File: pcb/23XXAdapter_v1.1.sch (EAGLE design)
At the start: 29 parts, among them IC1 23XX, IC2 EPROM, IC3 74HCT138N

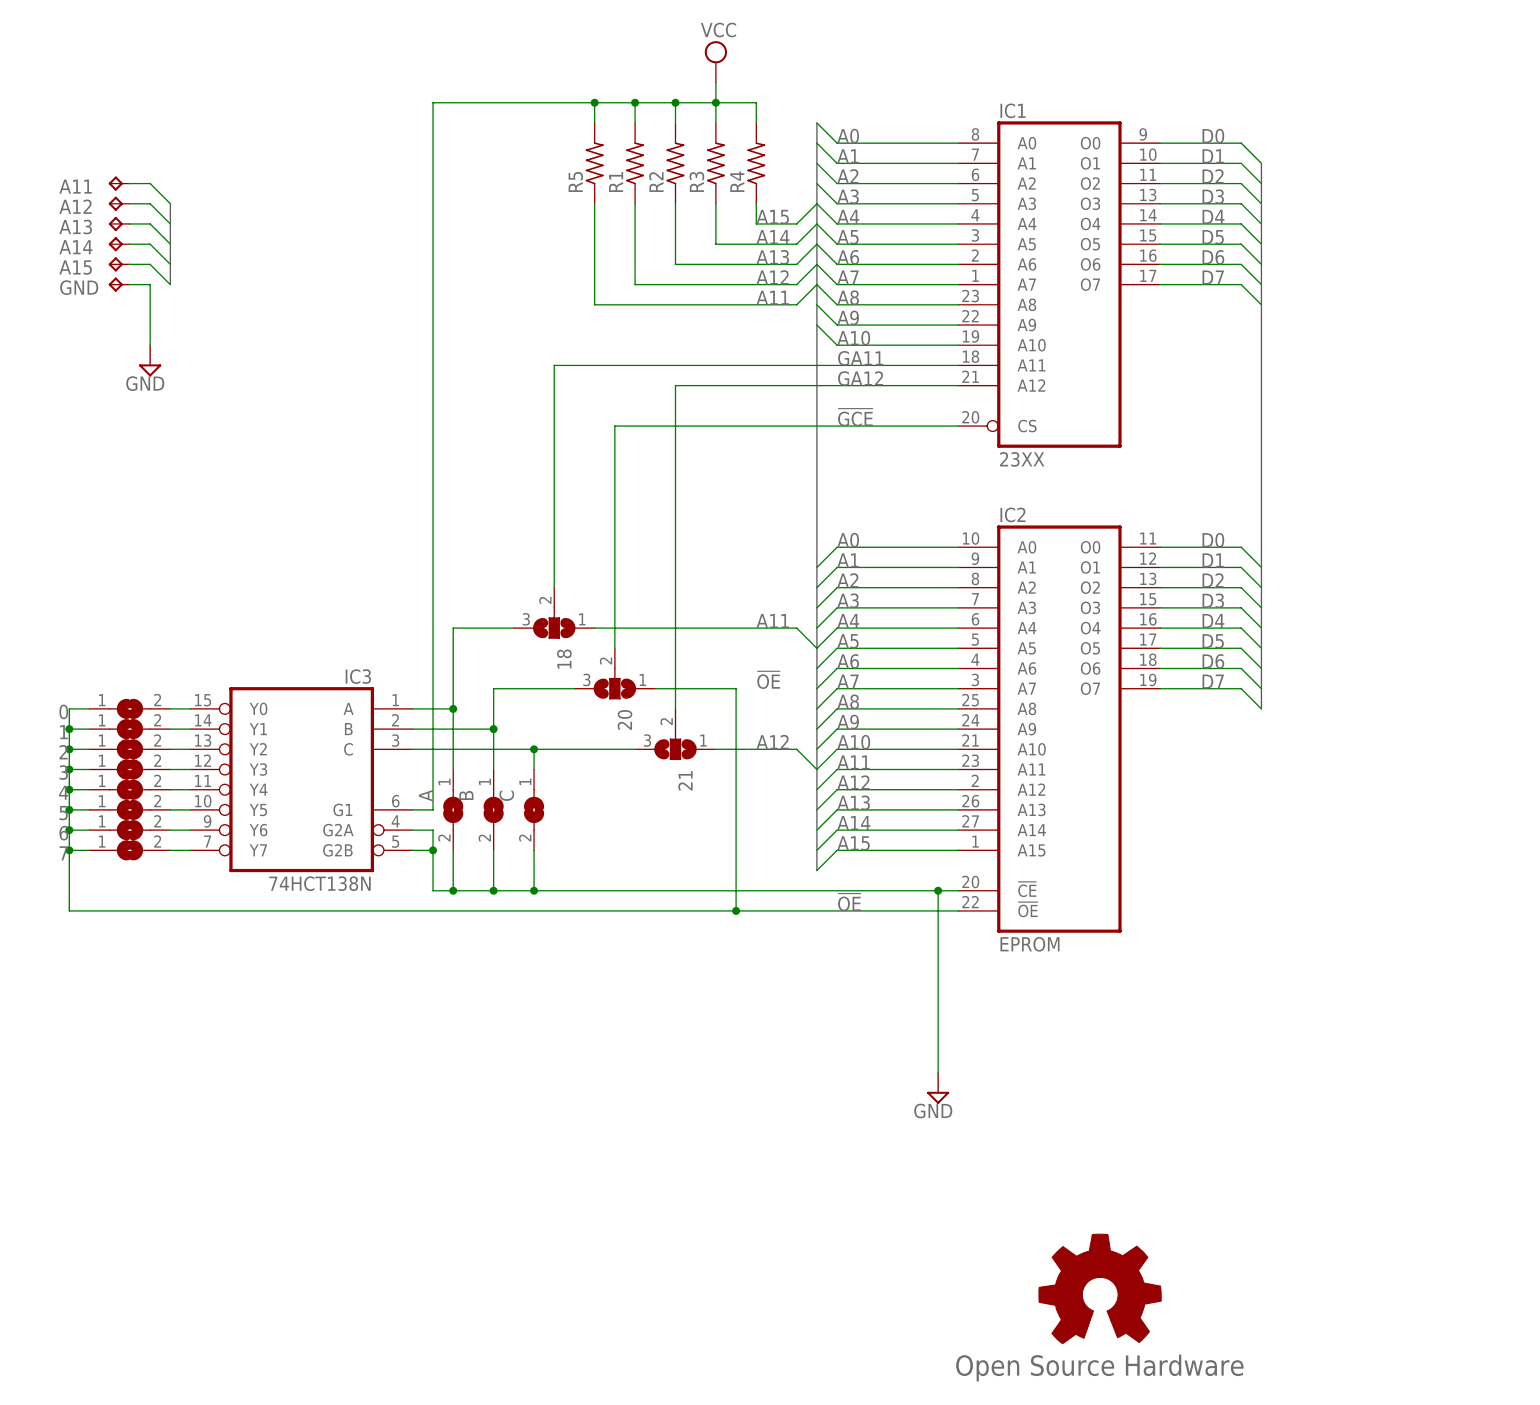
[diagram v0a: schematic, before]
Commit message: Added BOM and updates to PCB
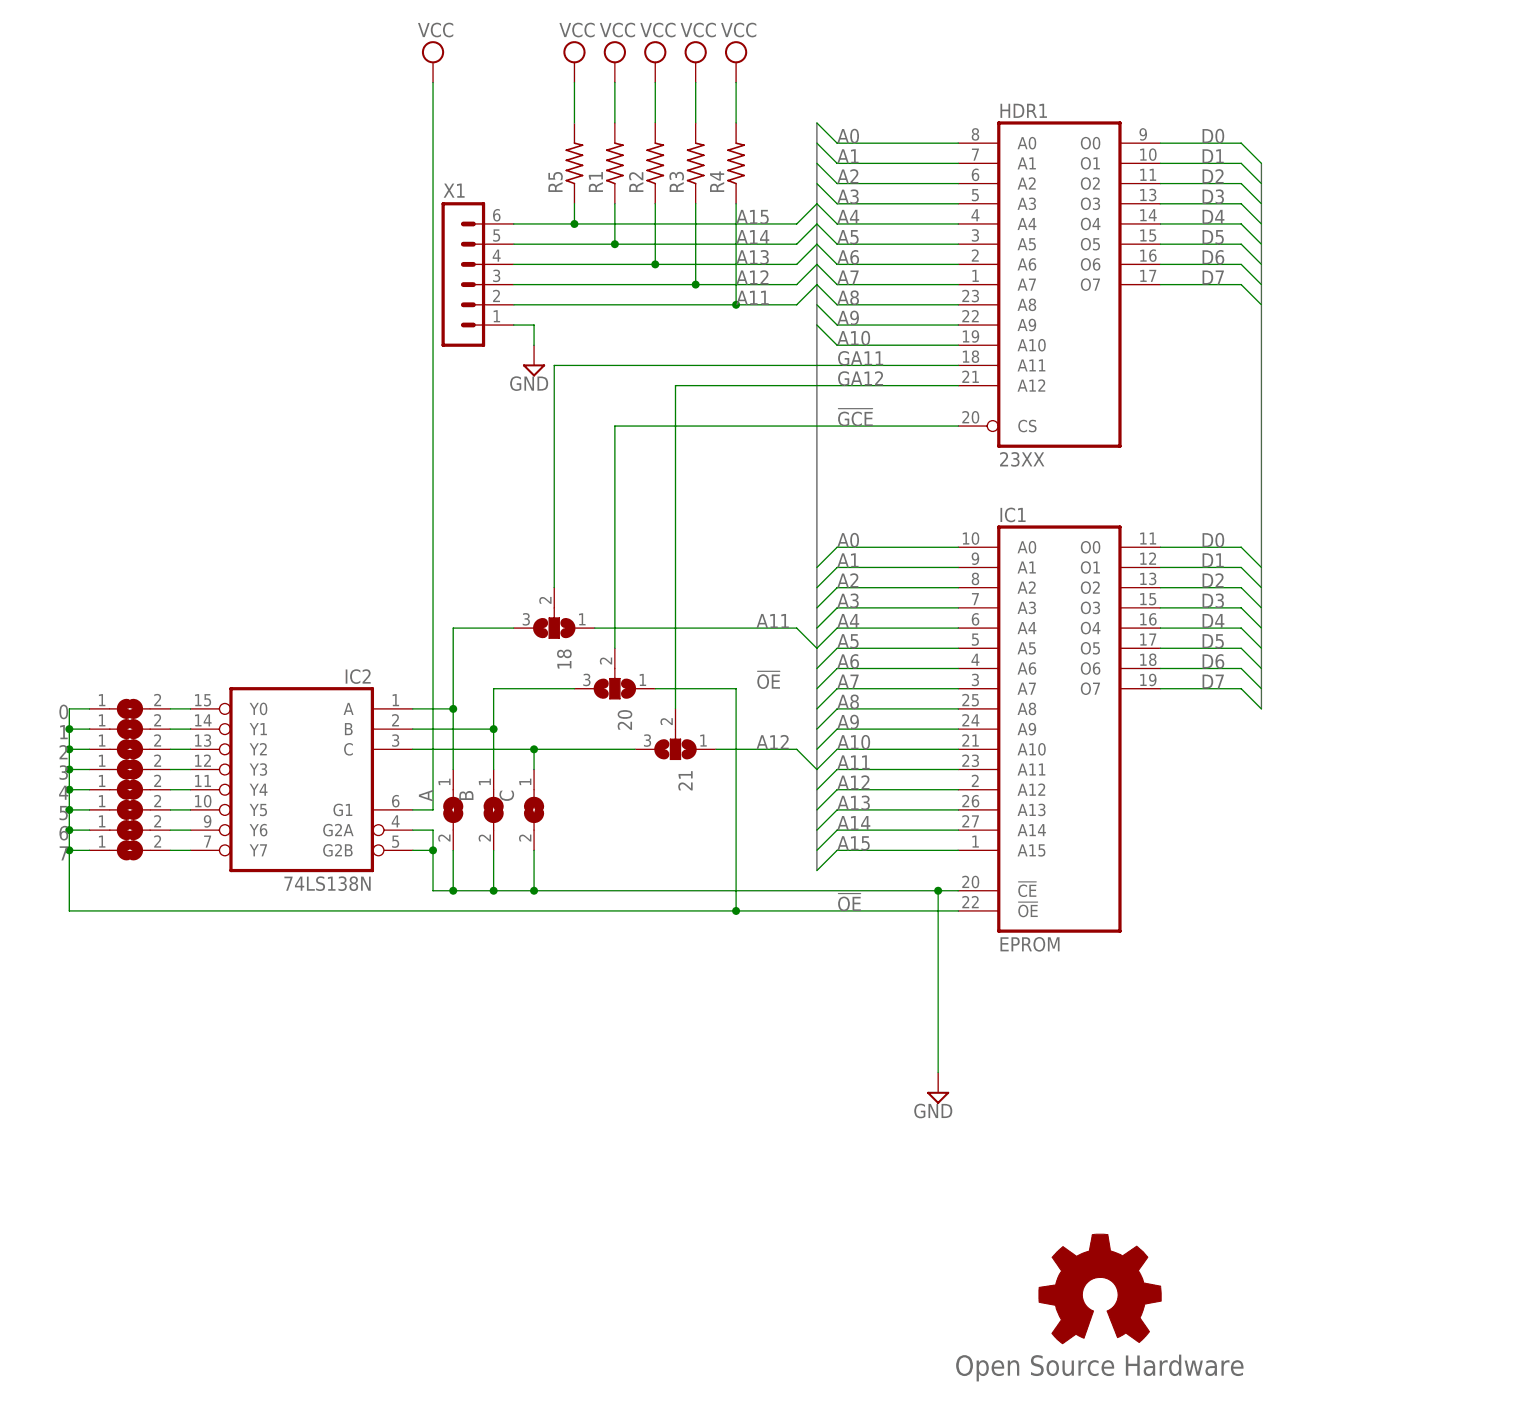
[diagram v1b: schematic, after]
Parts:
- removed A11, A12, A13, A14, A15, GND: TPTP12R, testpad:TPTP12R
- removed IC3: 74HCT138N, 74xx-us:74LS138N
- added HDR1: 23XX, 0RB_Memory:2364'RD'
- added X1: (no value), con-lstb-rp:MA06-1
- IC1: value 23XX -> EPROM; device 0RB_Memory:2364'RD' -> 0RB_Memory:27512'RD'
- IC2: value EPROM -> 74LS138N; device 0RB_Memory:27512'RD' -> 74xx-us-jlb:74LS138N
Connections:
- net !GCE: now also HDR1A.CS; no longer IC1A.CS
- net !OE: now also IC1G$1.!OE; no longer IC2G$1.!OE
- net A0: now also HDR1A.A0, IC1G$1.A0; no longer IC1A.A0, IC2G$1.A0
- net A1: now also HDR1A.A1, IC1G$1.A1; no longer IC1A.A1, IC2G$1.A1
- net A10: now also HDR1A.A10, IC1G$1.A10; no longer IC1A.A10, IC2G$1.A10
- net A11: now also IC1G$1.A11, X1.6; no longer A11.TP, IC2G$1.A11
- net A12: now also IC1G$1.A12, X1.5; no longer A12.TP, IC2G$1.A12
- net A13: now also IC1G$1.A13, X1.4; no longer A13.TP, IC2G$1.A13
- net A14: now also IC1G$1.A14, X1.3; no longer A14.TP, IC2G$1.A14
- net A15: now also IC1G$1.A15, X1.2; no longer A15.TP, IC2G$1.A15
- net A2: now also HDR1A.A2, IC1G$1.A2; no longer IC1A.A2, IC2G$1.A2
- net A3: now also HDR1A.A3, IC1G$1.A3; no longer IC1A.A3, IC2G$1.A3
- net A4: now also HDR1A.A4, IC1G$1.A4; no longer IC1A.A4, IC2G$1.A4
- net A5: now also HDR1A.A5, IC1G$1.A5; no longer IC1A.A5, IC2G$1.A5
- net A6: now also HDR1A.A6, IC1G$1.A6; no longer IC1A.A6, IC2G$1.A6
- net A7: now also HDR1A.A7, IC1G$1.A7; no longer IC1A.A7, IC2G$1.A7
- net A8: now also HDR1A.A8, IC1G$1.A8; no longer IC1A.A8, IC2G$1.A8
- net A9: now also HDR1A.A9, IC1G$1.A9; no longer IC1A.A9, IC2G$1.A9
- net D0: now also HDR1A.O0, IC1G$1.O0; no longer IC1A.O0, IC2G$1.O0
- net D1: now also HDR1A.O1, IC1G$1.O1; no longer IC1A.O1, IC2G$1.O1
- net D2: now also HDR1A.O2, IC1G$1.O2; no longer IC1A.O2, IC2G$1.O2
- net D3: now also HDR1A.O3, IC1G$1.O3; no longer IC1A.O3, IC2G$1.O3
- net D4: now also HDR1A.O4, IC1G$1.O4; no longer IC1A.O4, IC2G$1.O4
- net D5: now also HDR1A.O5, IC1G$1.O5; no longer IC1A.O5, IC2G$1.O5
- net D6: now also HDR1A.O6, IC1G$1.O6; no longer IC1A.O6, IC2G$1.O6
- net D7: now also HDR1A.O7, IC1G$1.O7; no longer IC1A.O7, IC2G$1.O7
- net GA11: now also HDR1A.A11; no longer IC1A.A11
- net GA12: now also HDR1A.A12; no longer IC1A.A12
- net GND: now also IC1G$1.!CE, IC2A.G2A, IC2A.G2B, X1.1; no longer GND.TP, IC2G$1.!CE, IC3A.G2A, IC3A.G2B
- net N$1: now also IC2A.B; no longer IC3A.B
- net N$10: now also IC2A.Y5; no longer IC3A.Y5
- net N$11: now also IC2A.Y6; no longer IC3A.Y6
- net N$12: now also IC2A.Y7; no longer IC3A.Y7
- net N$13: now also IC2A.C; no longer IC3A.C
- net N$16: now also IC2A.A; no longer IC3A.A
- net N$4: now also IC2A.Y0; no longer IC3A.Y0
- net N$6: now also IC2A.Y1; no longer IC3A.Y1
- net N$7: now also IC2A.Y2; no longer IC3A.Y2
- net N$8: now also IC2A.Y3; no longer IC3A.Y3
- net N$9: now also IC2A.Y4; no longer IC3A.Y4
- net VCC: now also IC2A.G1; no longer IC3A.G1
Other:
- moved on the sheet: R1, R2, R3, R4, R5

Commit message: Update schematic to show VCC/GND and pre-connected pads, h/t Mike Forster
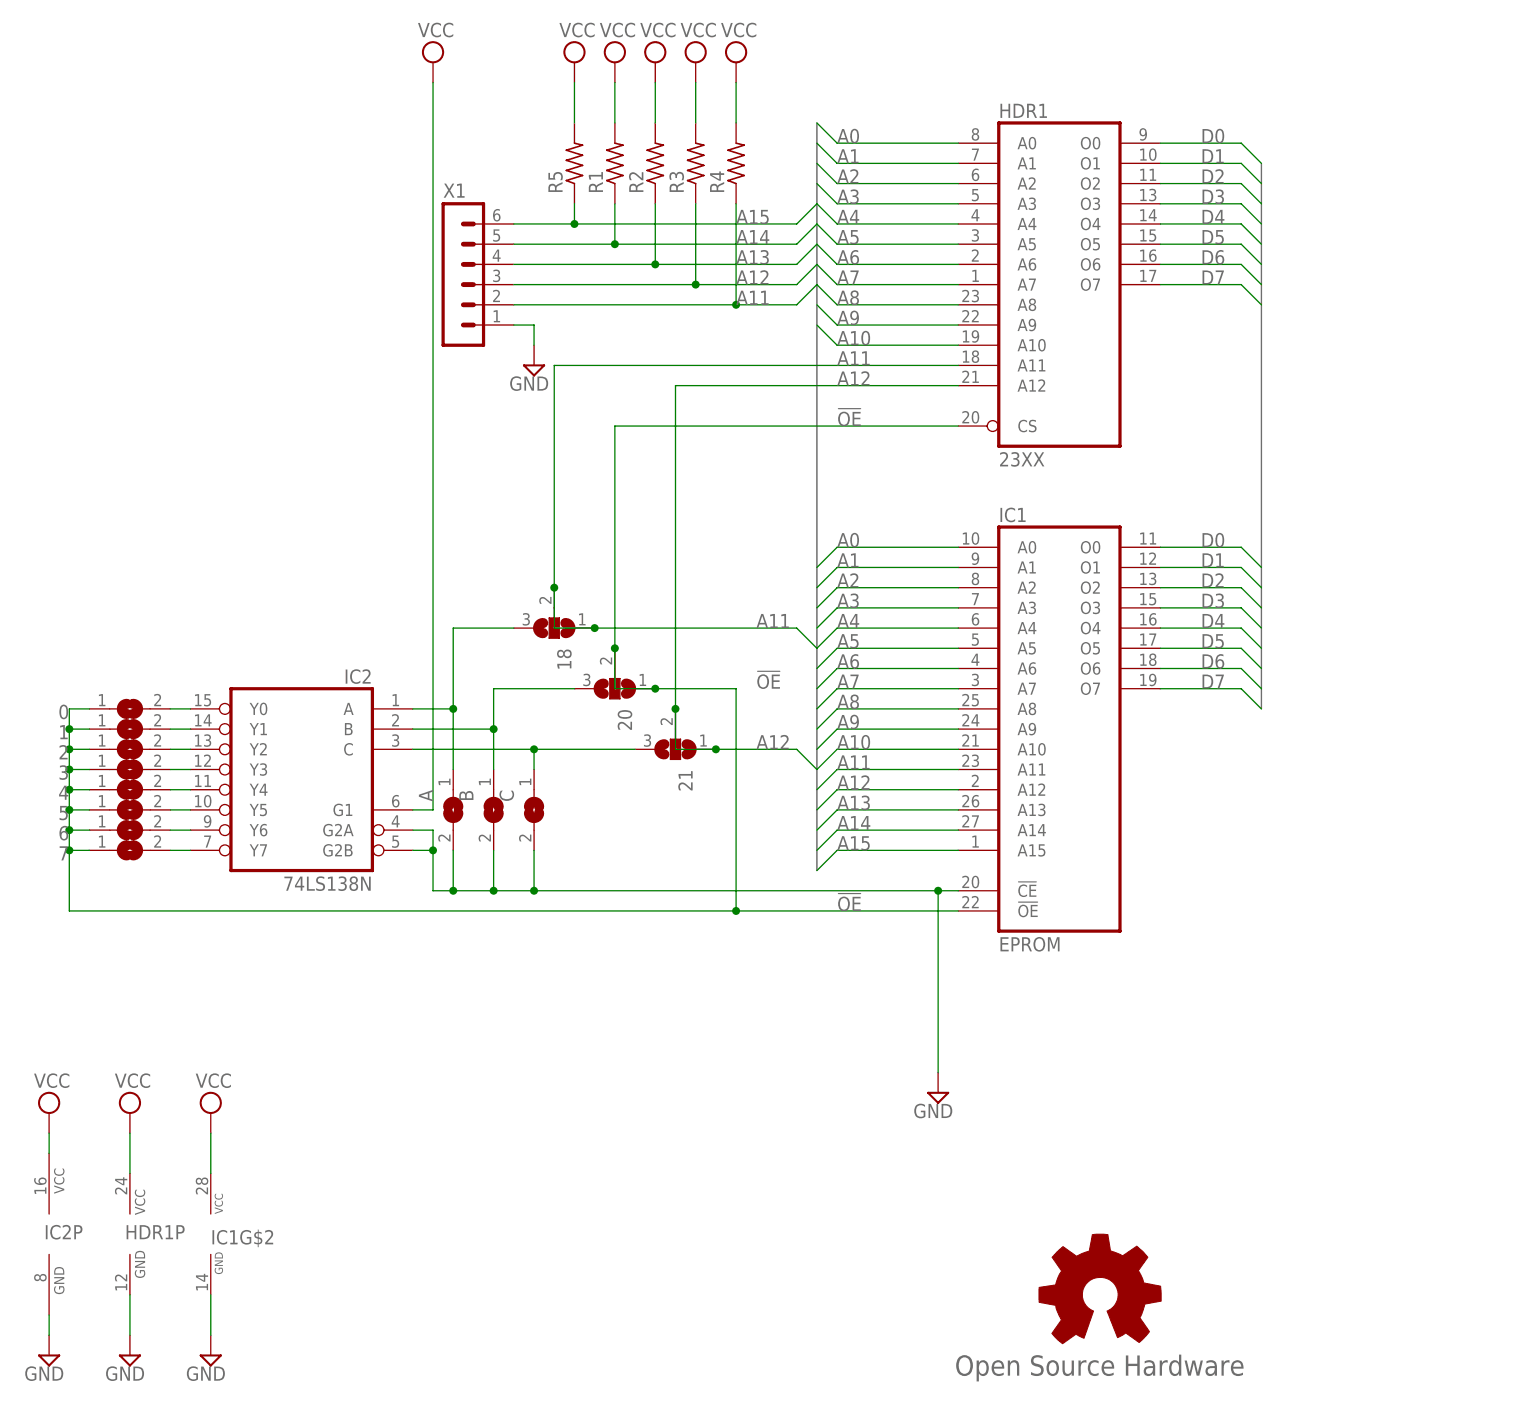
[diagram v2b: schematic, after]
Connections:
- removed net !GCE: 20.2, HDR1A.CS
- removed net GA11: 18.2, HDR1A.A11
- removed net GA12: 21.2, HDR1A.A12
- net !OE: now also 20.2, HDR1A.CS
- net A11: now also 18.2, HDR1A.A11
- net A12: now also 21.2, HDR1A.A12
- net GND: now also HDR1P.GND, IC1G$2.GND, IC2P.GND
- net VCC: now also HDR1P.VCC, IC1G$2.VCC, IC2P.VCC
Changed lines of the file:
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@@
 <part name="SUPPLY7" library="supply2" deviceset="VCC" device=""/>
 <part name="SUPPLY8" library="supply2" deviceset="VCC" device=""/>
+<part name="SUPPLY9" library="supply2" deviceset="VCC" device=""/>
+<part name="SUPPLY10" library="supply2" deviceset="VCC" device=""/>
+<part name="SUPPLY11" library="supply2" deviceset="VCC" device=""/>
+<part name="SUPPLY12" library="supply2" deviceset="GND" device=""/>
+<part name="SUPPLY13" library="supply2" deviceset="GND" device=""/>
+<part name="SUPPLY14" library="supply2" deviceset="GND" device=""/>
 </parts>
 <sheets>
@@
 <instance part="SUPPLY7" gate="G$1" x="81.28" y="167.64"/>
 <instance part="SUPPLY8" gate="G$1" x="91.44" y="167.64"/>
+<instance part="IC2" gate="P" x="5.08" y="20.32"/>
+<instance part="IC1" gate="G$2" x="25.4" y="20.32"/>
+<instance part="HDR1" gate="P" x="15.24" y="20.32"/>
+<instance part="SUPPLY9" gate="G$1" x="5.08" y="35.56"/>
+<instance part="SUPPLY10" gate="G$1" x="15.24" y="35.56"/>
+<instance part="SUPPLY11" gate="G$1" x="25.4" y="35.56"/>
+<instance part="SUPPLY12" gate="GND" x="5.08" y="5.08" rot="MR0"/>
+<instance part="SUPPLY13" gate="GND" x="15.24" y="5.08" rot="MR0"/>
+<instance part="SUPPLY14" gate="GND" x="25.4" y="5.08" rot="MR0"/>
 </instances>
 <busses>
@@
 <label x="93.98" y="96.52" size="1.778" layer="95"/>
 <pinref part="18" gate="G$1" pin="1"/>
+<wire x1="119.38" y1="129.54" x2="68.58" y2="129.54" width="0.1524" layer="91"/>
+<wire x1="68.58" y1="129.54" x2="68.58" y2="101.6" width="0.1524" layer="91"/>
+<label x="104.14" y="129.54" size="1.778" layer="95"/>
+<pinref part="HDR1" gate="A" pin="A11"/>
+<pinref part="18" gate="G$1" pin="2"/>
+<wire x1="73.66" y1="96.52" x2="68.58" y2="96.52" width="0.1524" layer="91"/>
+<wire x1="68.58" y1="96.52" x2="68.58" y2="101.6" width="0.1524" layer="91"/>
+<junction x="73.66" y="96.52"/>
+<junction x="68.58" y="101.6"/>
 </segment>
 <segment>
@@
 <label x="93.98" y="81.28" size="1.778" layer="95"/>
 <pinref part="21" gate="G$1" pin="1"/>
+<wire x1="119.38" y1="127" x2="83.82" y2="127" width="0.1524" layer="91"/>
+<wire x1="83.82" y1="127" x2="83.82" y2="86.36" width="0.1524" layer="91"/>
+<label x="104.14" y="127" size="1.778" layer="95"/>
+<pinref part="HDR1" gate="A" pin="A12"/>
+<pinref part="21" gate="G$1" pin="2"/>
+<wire x1="88.9" y1="81.28" x2="83.82" y2="81.28" width="0.1524" layer="91"/>
+<wire x1="83.82" y1="81.28" x2="83.82" y2="86.36" width="0.1524" layer="91"/>
+<junction x="88.9" y="81.28"/>
+<junction x="83.82" y="86.36"/>
 </segment>
 <segment>
@@
 <pinref part="X1" gate="1" pin="1"/>
 </segment>
+<segment>
+<pinref part="IC2" gate="P" pin="GND"/>
+<pinref part="SUPPLY12" gate="GND" pin="GND"/>
+<wire x1="5.08" y1="10.16" x2="5.08" y2="7.62" width="0.1524" layer="91"/>
+</segment>
+<segment>
+<pinref part="HDR1" gate="P" pin="GND"/>
+<pinref part="SUPPLY13" gate="GND" pin="GND"/>
+<wire x1="15.24" y1="12.7" x2="15.24" y2="7.62" width="0.1524" layer="91"/>
+</segment>
+<segment>
+<pinref part="IC1" gate="G$2" pin="GND"/>
+<pinref part="SUPPLY14" gate="GND" pin="GND"/>
+<wire x1="25.4" y1="12.7" x2="25.4" y2="7.62" width="0.1524" layer="91"/>
+</segment>
 </net>
 <net name="VCC" class="0">
@@
 <pinref part="IC2" gate="A" pin="G1"/>
 <pinref part="SUPPLY1" gate="G$1" pin="VCC"/>
+</segment>
+<segment>
+<pinref part="SUPPLY9" gate="G$1" pin="VCC"/>
+<pinref part="IC2" gate="P" pin="VCC"/>
+<wire x1="5.08" y1="33.02" x2="5.08" y2="30.48" width="0.1524" layer="91"/>
+</segment>
+<segment>
+<pinref part="SUPPLY10" gate="G$1" pin="VCC"/>
+<pinref part="HDR1" gate="P" pin="VCC"/>
+<wire x1="15.24" y1="33.02" x2="15.24" y2="27.94" width="0.1524" layer="91"/>
+</segment>
+<segment>
+<pinref part="SUPPLY11" gate="G$1" pin="VCC"/>
+<pinref part="IC1" gate="G$2" pin="VCC"/>
+<wire x1="25.4" y1="33.02" x2="25.4" y2="27.94" width="0.1524" layer="91"/>
 </segment>
 </net>
@@
 <wire x1="63.5" y1="137.16" x2="91.44" y2="137.16" width="0.1524" layer="91"/>
 <junction x="91.44" y="137.16"/>
-</segment>
-</net>
-<net name="GA12" class="0">
-<segment>
-<wire x1="119.38" y1="127" x2="83.82" y2="127" width="0.1524" layer="91"/>
-<wire x1="83.82" y1="127" x2="83.82" y2="86.36" width="0.1524" layer="91"/>
-<label x="104.14" y="127" size="1.778" layer="95"/>
-<pinref part="HDR1" gate="A" pin="A12"/>
-<pinref part="21" gate="G$1" pin="2"/>
 </segment>
 </net>
@@
 <pinref part="IC1" gate="G$1" pin="!OE"/>
 <pinref part="20" gate="G$1" pin="1"/>
+<wire x1="119.38" y1="121.92" x2="76.2" y2="121.92" width="0.1524" layer="91"/>
+<wire x1="76.2" y1="121.92" x2="76.2" y2="93.98" width="0.1524" layer="91"/>
+<label x="104.14" y="121.92" size="1.778" layer="95"/>
+<pinref part="HDR1" gate="A" pin="CS"/>
+<pinref part="20" gate="G$1" pin="2"/>
+<wire x1="81.28" y1="88.9" x2="76.2" y2="88.9" width="0.1524" layer="91"/>
+<wire x1="76.2" y1="88.9" x2="76.2" y2="93.98" width="0.1524" layer="91"/>
+<junction x="81.28" y="88.9"/>
+<junction x="76.2" y="93.98"/>
 </segment>
 </net>
@@
 <pinref part="C" gate="1" pin="1"/>
 <pinref part="IC2" gate="A" pin="C"/>
-</segment>
-</net>
-<net name="!GCE" class="0">
-<segment>
-<wire x1="119.38" y1="121.92" x2="76.2" y2="121.92" width="0.1524" layer="91"/>
-<wire x1="76.2" y1="121.92" x2="76.2" y2="93.98" width="0.1524" layer="91"/>
-<label x="104.14" y="121.92" size="1.778" layer="95"/>
-<pinref part="HDR1" gate="A" pin="CS"/>
-<pinref part="20" gate="G$1" pin="2"/>
 </segment>
 </net>
@@
 </segment>
 </net>
-<net name="GA11" class="0">
-<segment>
-<wire x1="119.38" y1="129.54" x2="68.58" y2="129.54" width="0.1524" layer="91"/>
-<wire x1="68.58" y1="129.54" x2="68.58" y2="101.6" width="0.1524" layer="91"/>
-<label x="104.14" y="129.54" size="1.778" layer="95"/>
-<pinref part="HDR1" gate="A" pin="A11"/>
-<pinref part="18" gate="G$1" pin="2"/>
-</segment>
-</net>
